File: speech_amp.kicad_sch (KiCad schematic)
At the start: 48 parts, among them Q1701 MMBT3906, Q1702 MMBT3904, Q1703 MMBT3904, U1701 LMC6482

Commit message: Update pcb database to version 6
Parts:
- C1701, C1705, C1706, C1710: symbol Custom:C_US_0805_0.1UF_X7R_10%_50V_HS -> custom:C_US_0805_0.1UF_X7R_10%_50V_HS
- C1702: symbol Custom:CP_US -> custom:CP_US; PartNumber 800268-107 -> 80000X-XXX
- C1703, C1707, C1708, C1711, C1716: symbol Custom:CP_US -> custom:CP_US; PartNumber 800267-226 -> 80000X-XXX
- C1704: footprint Capacitor_SMD:C_0805_2012Metric_Pad1.15x1.40mm_HandSolder -> Capacitor_SMD:C_0603_1608Metric; symbol Custom:C_US -> custom:C_US; PartNumber 800239-103 -> 800063-XXX
- C1709, C1712, C1713, C1714, C1715: footprint Capacitor_SMD:C_0805_2012Metric_Pad1.15x1.40mm_HandSolder -> Capacitor_SMD:C_0603_1608Metric; symbol Custom:C_US -> custom:C_US; PartNumber 800239-272 -> 800063-XXX
- C1717: symbol Custom:C_US_0805_0.1UF_X7R_10%_50V_HS -> custom:C_US_0805_0.1UF_X7R_10%_50V_HS; PartNumber 800238-103 -> 800238-104
- Q1701: footprint mods:SOT23-3-SAR -> Package_TO_SOT_SMD:SOT-23; symbol Transistor_BJT:MMBT3906 -> custom:MMBT3906
- Q1702, Q1703: symbol Custom:MMBT3904 -> custom:MMBT3904
- R1701, R1718: symbol Custom:R_US_0805_1%_HS -> custom:R_US_0805_1%_HS; PartNumber 800235-101 -> 800235-XXX
- R1702, R1703, R1704, R1706, R1707, R1724: symbol Custom:R_US_0805_1%_HS -> custom:R_US_0805_1%_HS; PartNumber 800235-103 -> 800235-XXX
- R1705, R1713: symbol Custom:POT_US -> custom:POT_US
- R1708: symbol Custom:R_US_0805_1%_HS -> custom:R_US_0805_1%_HS; PartNumber 800235-681 -> 800235-XXX
- R1709: symbol Custom:R_US_0805_1%_HS -> custom:R_US_0805_1%_HS; PartNumber 800235-202 -> 800235-XXX
- R1710: symbol Custom:R_US_0805_1%_HS -> custom:R_US_0805_1%_HS; PartNumber 800235-274 -> 800235-XXX
- R1711: symbol Custom:R_US_0805_1%_HS -> custom:R_US_0805_1%_HS; PartNumber 800235-104 -> 800235-XXX
- R1712: symbol Custom:R_US_0805_1%_HS -> custom:R_US_0805_1%_HS; PartNumber 800235-102 -> 800235-XXX
- R1714, R1717, R1719, R1720, R1721, R1722, R1725: symbol Custom:R_US_0805_1%_HS -> custom:R_US_0805_1%_HS; PartNumber 800235-473 -> 800235-XXX
- R1715: symbol Custom:R_US_0805_1%_HS -> custom:R_US_0805_1%_HS; PartNumber 800235-753 -> 800235-XXX
- R1716: symbol Custom:R_US_0805_1%_HS -> custom:R_US_0805_1%_HS; PartNumber 800235-223 -> 800235-XXX
- R1723: symbol Custom:R_US_0805_1%_HS -> custom:R_US_0805_1%_HS; PartNumber 800235-393 -> 800235-XXX
- TP1701, TP1702: footprint mods:TESTPIN -> TESTPIN; symbol Custom:TESTPINTPSQ025 -> custom:TESTPINTPSQ025
- U1701: symbol Custom:LMC6482 -> custom:LMC6482

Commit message: Fix BOM part number errors and out of sync footprints which happened during conversion from Kicad 5 to 6
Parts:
- C1702: PartNumber 80000X-XXX -> 800268-107
- C1703, C1707, C1708, C1711, C1716: PartNumber 80000X-XXX -> 800267-226
- C1704: footprint Capacitor_SMD:C_0603_1608Metric -> Capacitor_SMD:C_0805_2012Metric_Pad1.15x1.40mm_HandSolder; PartNumber 800063-XXX -> 800239-103
- C1709, C1712, C1713, C1714, C1715: footprint Capacitor_SMD:C_0603_1608Metric -> Capacitor_SMD:C_0805_2012Metric_Pad1.15x1.40mm_HandSolder; PartNumber 800063-XXX -> 800239-272
- C1717: PartNumber 800238-104 -> 800239-103
- Q1701: footprint Package_TO_SOT_SMD:SOT-23 -> mods:SOT23-3-SAR
- R1701, R1718: PartNumber 800235-XXX -> 800235-101
- R1702, R1703, R1704, R1706, R1707, R1724: PartNumber 800235-XXX -> 800235-103
- R1708: PartNumber 800235-XXX -> 800235-681
- R1709: PartNumber 800235-XXX -> 800235-202
- R1710: PartNumber 800235-XXX -> 800235-274
- R1711: PartNumber 800235-XXX -> 800235-104
- R1712: PartNumber 800235-XXX -> 800235-102
- R1714, R1717, R1719, R1720, R1721, R1722, R1725: PartNumber 800235-XXX -> 800235-473
- R1715: PartNumber 800235-XXX -> 800235-753
- R1716: PartNumber 800235-XXX -> 800235-223
- R1723: PartNumber 800235-XXX -> 800235-393
- TP1701, TP1702: footprint TESTPIN -> mods:TESTPIN

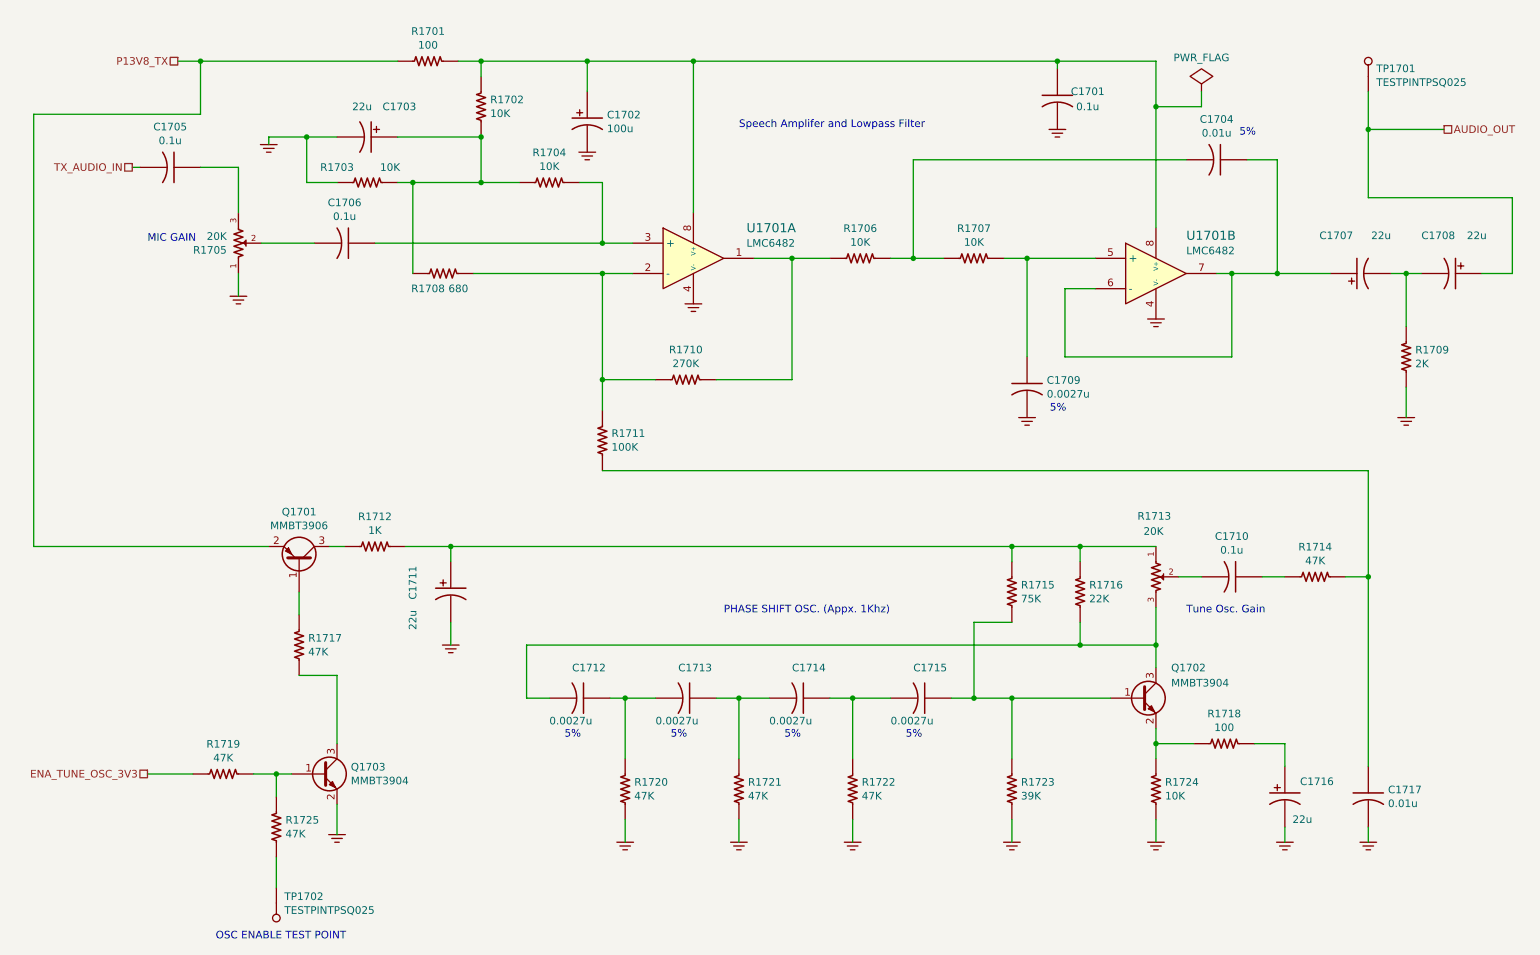
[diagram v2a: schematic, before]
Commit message: trx_mobo_concept_2_B. Change design to use a dedicated 8V supply for the 2SC3357 parts. Add S-Meter connector. Change mic connector to 3 pins and add 8V sopower supply to pin 3.
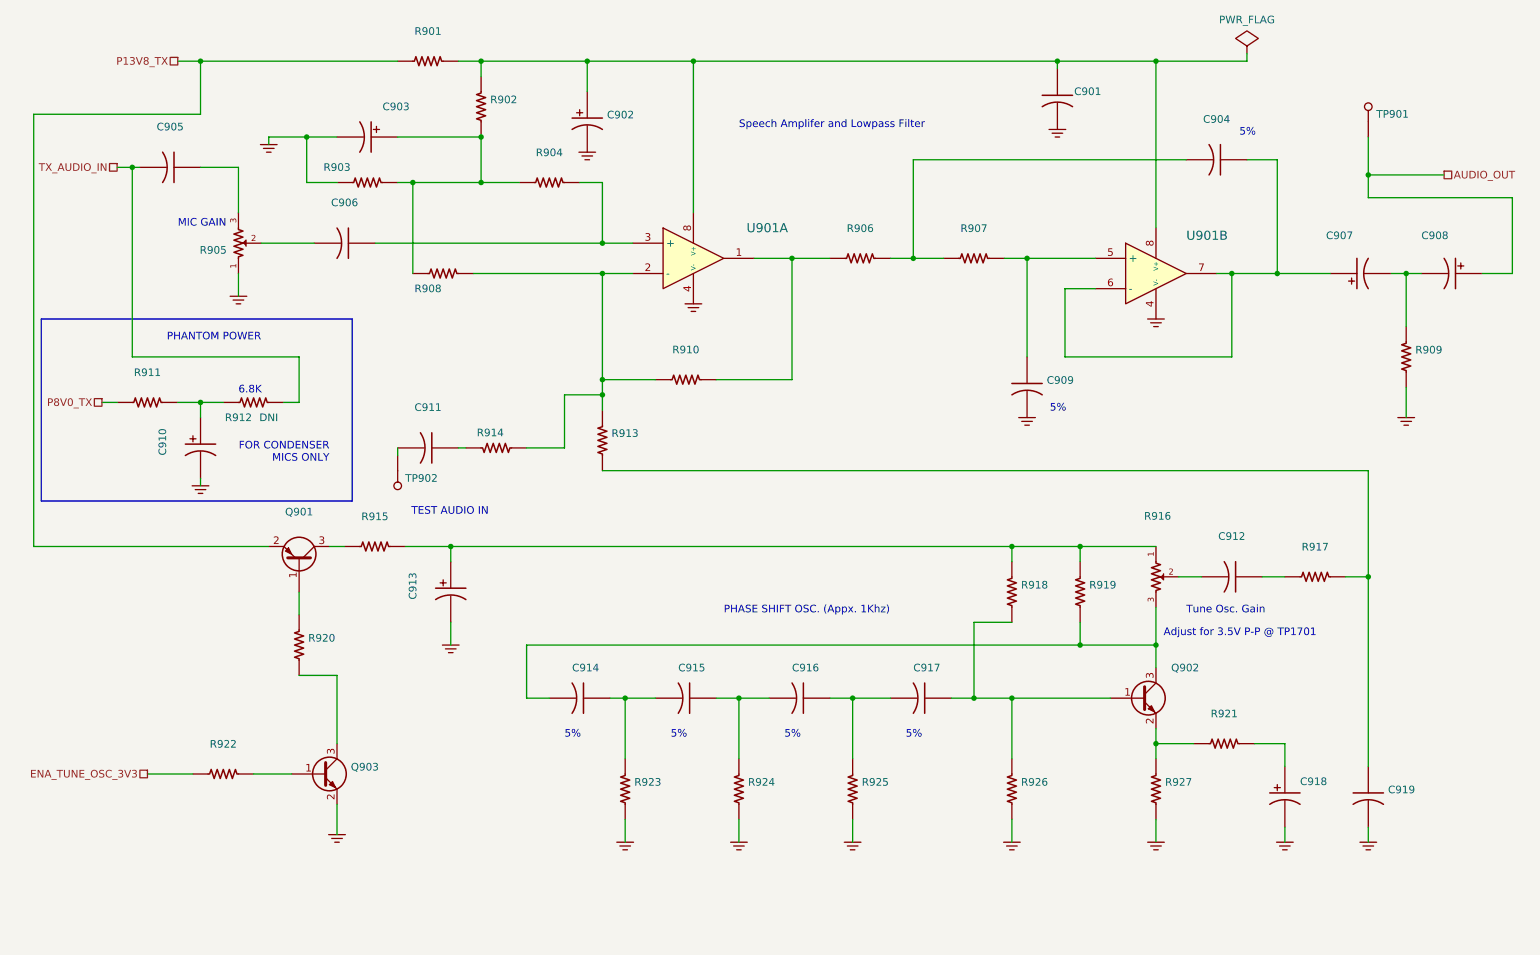
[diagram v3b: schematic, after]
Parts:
- removed R1725: 47K, Resistor_SMD:R_0805_2012Metric_Pad1.15x1.40mm_HandSolder, symbol custom:R_US_0805_1%_HS
- added C910: (no value), symbol custom:CP_US
- added C911: (no value), symbol custom:C_US_0805_0.1UF_X7R_10%_50V_HS
- added R911, R914: (no value), symbol custom:R_US_0805_1%_HS
- added R912: DNI, symbol custom:R_US_0805_1%_HS
- C901: renamed from C1701; value 0.1u -> (none); footprint Capacitor_SMD:C_0805_2012Metric_Pad1.15x1.40mm_HandSolder -> (none)
- C902: renamed from C1702; value 100u -> (none); footprint Capacitor_SMD:CP_Elec_8x10 -> (none)
- C903: renamed from C1703; value 22u -> (none); footprint Capacitor_SMD:CP_Elec_6.3x5.7 -> (none)
- C904: renamed from C1704; value 0.01u -> (none); footprint Capacitor_SMD:C_0805_2012Metric_Pad1.15x1.40mm_HandSolder -> (none)
- C905: renamed from C1705; value 0.1u -> (none); footprint Capacitor_SMD:C_0805_2012Metric_Pad1.15x1.40mm_HandSolder -> (none)
- C906: renamed from C1706; value 0.1u -> (none); footprint Capacitor_SMD:C_0805_2012Metric_Pad1.15x1.40mm_HandSolder -> (none)
- C907: renamed from C1707; value 22u -> (none); footprint Capacitor_SMD:CP_Elec_6.3x5.7 -> (none)
- C908: renamed from C1708; value 22u -> (none); footprint Capacitor_SMD:CP_Elec_6.3x5.7 -> (none)
- C909: renamed from C1709; value 0.0027u -> (none); footprint Capacitor_SMD:C_0805_2012Metric_Pad1.15x1.40mm_HandSolder -> (none)
- C912: renamed from C1710; value 0.1u -> (none); footprint Capacitor_SMD:C_0805_2012Metric_Pad1.15x1.40mm_HandSolder -> (none)
- C913: renamed from C1711; value 22u -> (none); footprint Capacitor_SMD:CP_Elec_6.3x5.7 -> (none)
- C914: renamed from C1712; value 0.0027u -> (none); footprint Capacitor_SMD:C_0805_2012Metric_Pad1.15x1.40mm_HandSolder -> (none)
- C915: renamed from C1713; value 0.0027u -> (none); footprint Capacitor_SMD:C_0805_2012Metric_Pad1.15x1.40mm_HandSolder -> (none)
- C916: renamed from C1714; value 0.0027u -> (none); footprint Capacitor_SMD:C_0805_2012Metric_Pad1.15x1.40mm_HandSolder -> (none)
- C917: renamed from C1715; value 0.0027u -> (none); footprint Capacitor_SMD:C_0805_2012Metric_Pad1.15x1.40mm_HandSolder -> (none)
- C918: renamed from C1716; value 22u -> (none); footprint Capacitor_SMD:CP_Elec_6.3x5.7 -> (none)
- C919: renamed from C1717; value 0.01u -> (none); footprint Capacitor_SMD:C_0805_2012Metric_Pad1.15x1.40mm_HandSolder -> (none)
- Q901: renamed from Q1701; value MMBT3906 -> (none); footprint mods:SOT23-3-SAR -> (none)
- Q902: renamed from Q1702; value MMBT3904 -> (none); footprint mods:SOT23-3-SAR -> (none)
- Q903: renamed from Q1703; value MMBT3904 -> (none); footprint mods:SOT23-3-SAR -> (none)
- R901: renamed from R1701; value 100 -> (none); footprint Resistor_SMD:R_0805_2012Metric_Pad1.15x1.40mm_HandSolder -> (none)
- R902: renamed from R1702; value 10K -> (none); footprint Resistor_SMD:R_0805_2012Metric_Pad1.15x1.40mm_HandSolder -> (none)
- R903: renamed from R1703; value 10K -> (none); footprint Resistor_SMD:R_0805_2012Metric_Pad1.15x1.40mm_HandSolder -> (none)
- R904: renamed from R1704; value 10K -> (none); footprint Resistor_SMD:R_0805_2012Metric_Pad1.15x1.40mm_HandSolder -> (none)
- R905: renamed from R1705; value 20K -> (none); footprint mods:Potentiometer_Bourns_3296W_Vertical_Screw_SS -> (none)
- R906: renamed from R1706; value 10K -> (none); footprint Resistor_SMD:R_0805_2012Metric_Pad1.15x1.40mm_HandSolder -> (none)
- R907: renamed from R1707; value 10K -> (none); footprint Resistor_SMD:R_0805_2012Metric_Pad1.15x1.40mm_HandSolder -> (none)
- R908: renamed from R1708; value 680 -> (none); footprint Resistor_SMD:R_0805_2012Metric_Pad1.15x1.40mm_HandSolder -> (none)
- R909: renamed from R1709; value 2K -> (none); footprint Resistor_SMD:R_0805_2012Metric_Pad1.15x1.40mm_HandSolder -> (none)
- R910: renamed from R1710; value 270K -> (none); footprint Resistor_SMD:R_0805_2012Metric_Pad1.15x1.40mm_HandSolder -> (none)
- R913: renamed from R1711; value 100K -> (none); footprint Resistor_SMD:R_0805_2012Metric_Pad1.15x1.40mm_HandSolder -> (none)
- R915: renamed from R1712; value 1K -> (none); footprint Resistor_SMD:R_0805_2012Metric_Pad1.15x1.40mm_HandSolder -> (none)
- R916: renamed from R1713; value 20K -> (none); footprint mods:Potentiometer_Bourns_3296W_Vertical_Screw_SS -> (none)
- R917: renamed from R1714; value 47K -> (none); footprint Resistor_SMD:R_0805_2012Metric_Pad1.15x1.40mm_HandSolder -> (none)
- R918: renamed from R1715; value 75K -> (none); footprint Resistor_SMD:R_0805_2012Metric_Pad1.15x1.40mm_HandSolder -> (none)
- R919: renamed from R1716; value 22K -> (none); footprint Resistor_SMD:R_0805_2012Metric_Pad1.15x1.40mm_HandSolder -> (none)
- R920: renamed from R1717; value 47K -> (none); footprint Resistor_SMD:R_0805_2012Metric_Pad1.15x1.40mm_HandSolder -> (none)
- R921: renamed from R1718; value 100 -> (none); footprint Resistor_SMD:R_0805_2012Metric_Pad1.15x1.40mm_HandSolder -> (none)
- R922: renamed from R1719; value 47K -> (none); footprint Resistor_SMD:R_0805_2012Metric_Pad1.15x1.40mm_HandSolder -> (none)
- R923: renamed from R1720; value 47K -> (none); footprint Resistor_SMD:R_0805_2012Metric_Pad1.15x1.40mm_HandSolder -> (none)
- R924: renamed from R1721; value 47K -> (none); footprint Resistor_SMD:R_0805_2012Metric_Pad1.15x1.40mm_HandSolder -> (none)
- R925: renamed from R1722; value 47K -> (none); footprint Resistor_SMD:R_0805_2012Metric_Pad1.15x1.40mm_HandSolder -> (none)
- R926: renamed from R1723; value 39K -> (none); footprint Resistor_SMD:R_0805_2012Metric_Pad1.15x1.40mm_HandSolder -> (none)
- R927: renamed from R1724; value 10K -> (none); footprint Resistor_SMD:R_0805_2012Metric_Pad1.15x1.40mm_HandSolder -> (none)
- TP901: renamed from TP1701; value TESTPINTPSQ025 -> (none); footprint mods:TESTPIN -> (none)
- TP902: renamed from TP1702; value TESTPINTPSQ025 -> (none); footprint mods:TESTPIN -> (none)
- U901: renamed from U1701; value LMC6482 -> (none); footprint mods:SOIC8N-SAR -> (none)
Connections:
- net GND: now also C910.2
- net TX_AUDIO_IN: now also R912.1
- net at R908.1, R910.2, R913.1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: now also R914.2
- net at TP902.1 (TP): now also C911.2
- new net: C910.1, R911.1, R912.2
- new net: C911.1, R914.1
- new net P8V0_TX: R911.2
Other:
- note added: "6.8K"
- note added: "Adjust for 3.5V P-P @ TP1701"
- note added: "FOR CONDENSER MICS ONLY"
- note added: "PHANTOM POWER"
- note added: "TEST AUDIO IN"
- note removed: "OSC ENABLE TEST POINT"
- moved on the sheet: TP901, TP902

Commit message: Fix 12.288MHz part number in schematic, regenerate BOM's.
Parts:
- R912: value DNI -> (none)
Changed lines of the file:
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@@
     (in_bom yes) (on_board yes)
     (property "Reference" "R912" (id 0) (at 48.26 80.01 90))
-    (property "Value" "DNI" (id 1) (at 53.34 80.01 90))
+    (property "Value" "" (id 1) (at 53.34 80.01 90))
     (property "Footprint" "" (id 2) (at 50.8 77.47 0)
       (effects (font (size 1.524 1.524)) hide)
